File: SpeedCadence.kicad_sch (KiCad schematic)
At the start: 9 parts, among them SW1 SW_Push, U1 STM32F072RBTx

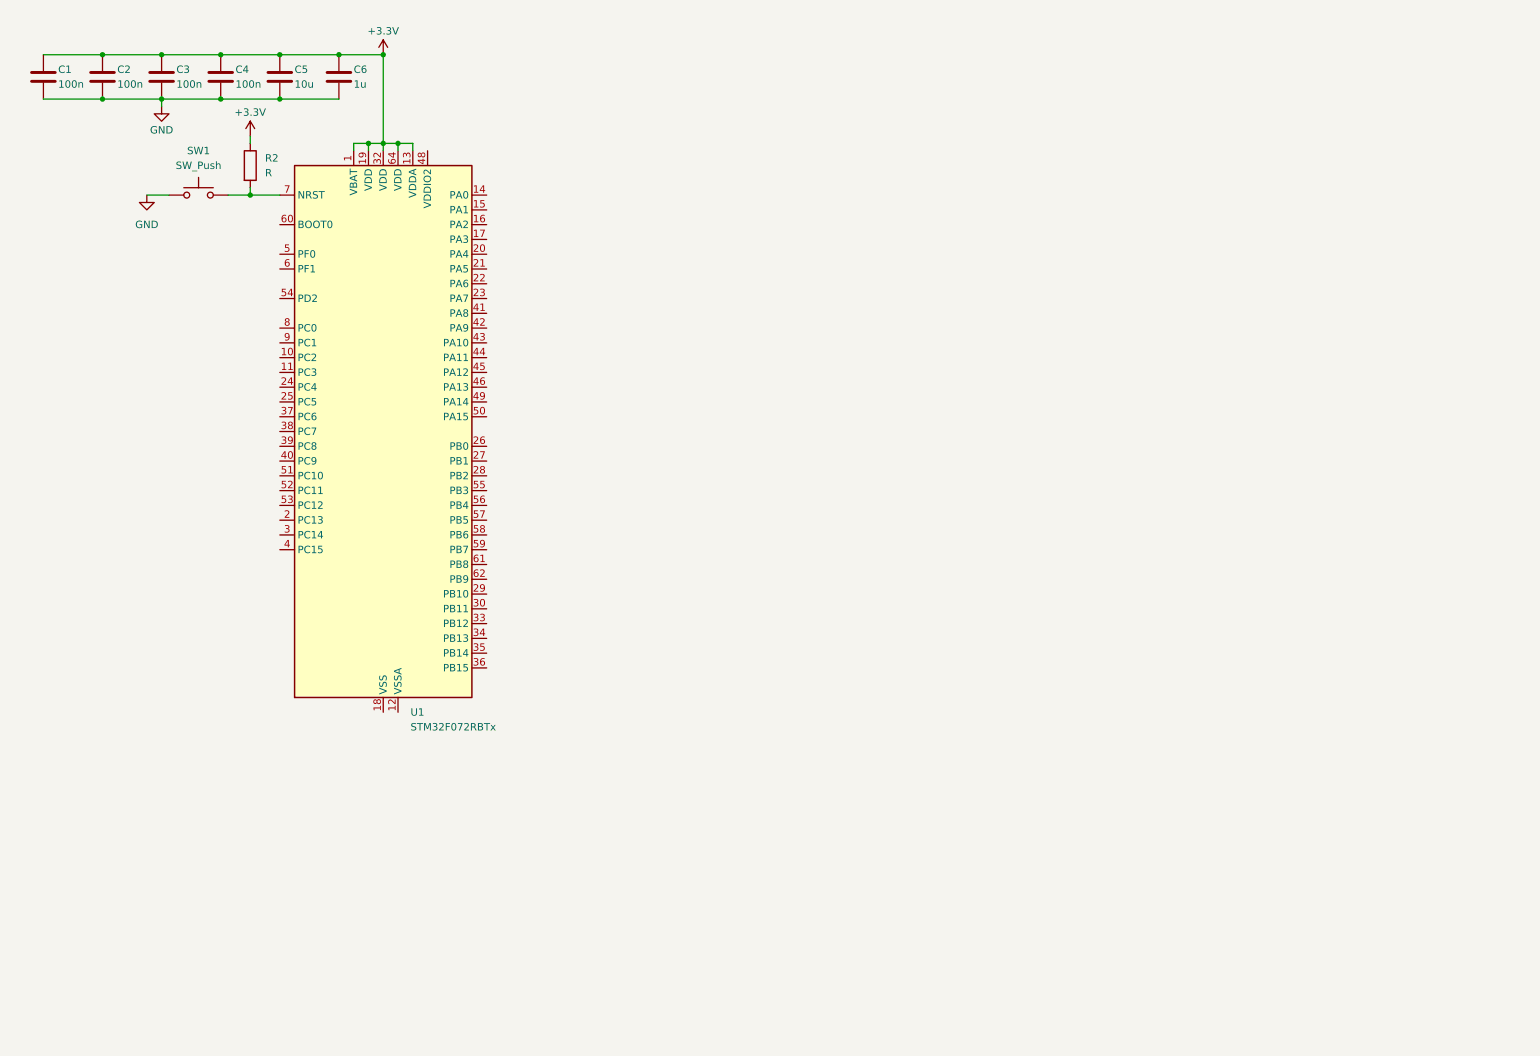
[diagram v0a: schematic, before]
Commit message: Added MCU
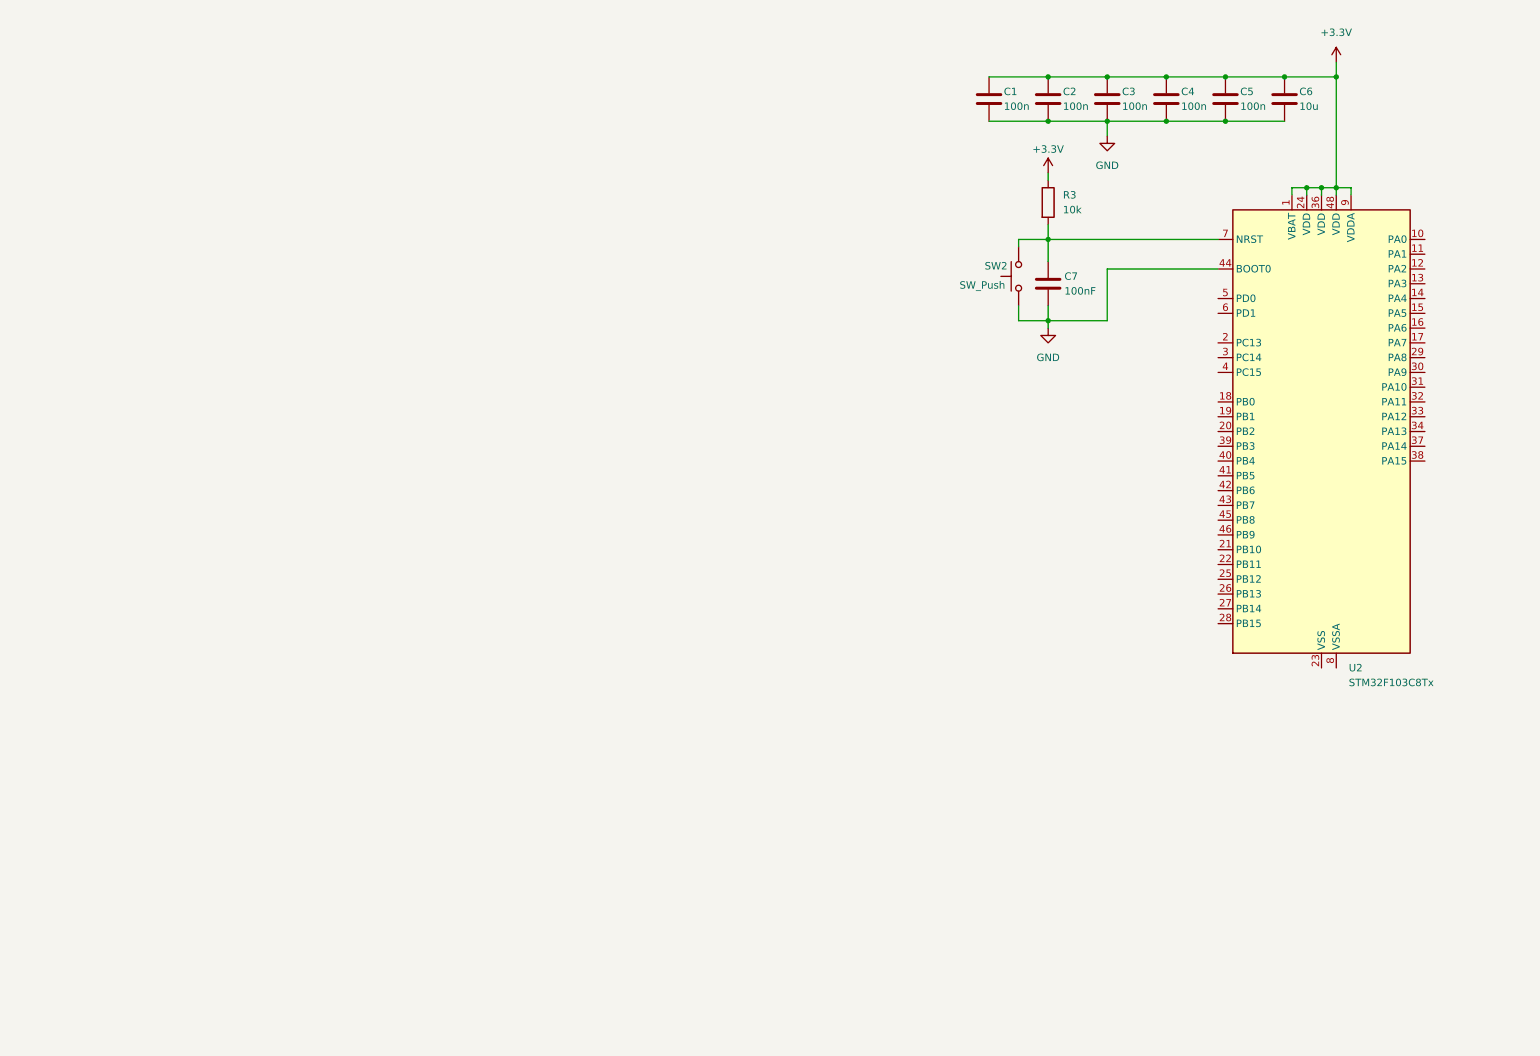
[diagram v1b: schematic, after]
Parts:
- removed R2: R, symbol Device:R
- removed SW1: SW_Push, symbol Switch:SW_Push
- removed U1: STM32F072RBTx, Package_QFP:LQFP-64_10x10mm_P0.5mm, symbol MCU_ST_STM32F0:STM32F072RBTx
- added C7: 100nF, symbol Device:C
- added R3: 10k, symbol Device:R
- added SW2: SW_Push, symbol Switch:SW_Push
- added U2: STM32F103C8Tx, Package_QFP:LQFP-48_7x7mm_P0.5mm, symbol MCU_ST_STM32F1:STM32F103C8Tx
- C5: value 10u -> 100n
- C6: value 1u -> 10u
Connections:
- net +3.3V: now also R3.1, U2.1 (VBAT), U2.24 (VDD), U2.36 (VDD), U2.48 (VDD), U2.9 (VDDA)
- net GND: now also C7.2, SW2.1, U2.44 (BOOT0)
- new net: U2.23 (VSS), U2.35 (VSS), U2.47 (VSS)
- new net: C7.1, R3.2, SW2.2, U2.7 (NRST)
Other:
- moved on the sheet: C1, C2, C3, C4, C5, C6

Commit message: Added connecter and hall effect
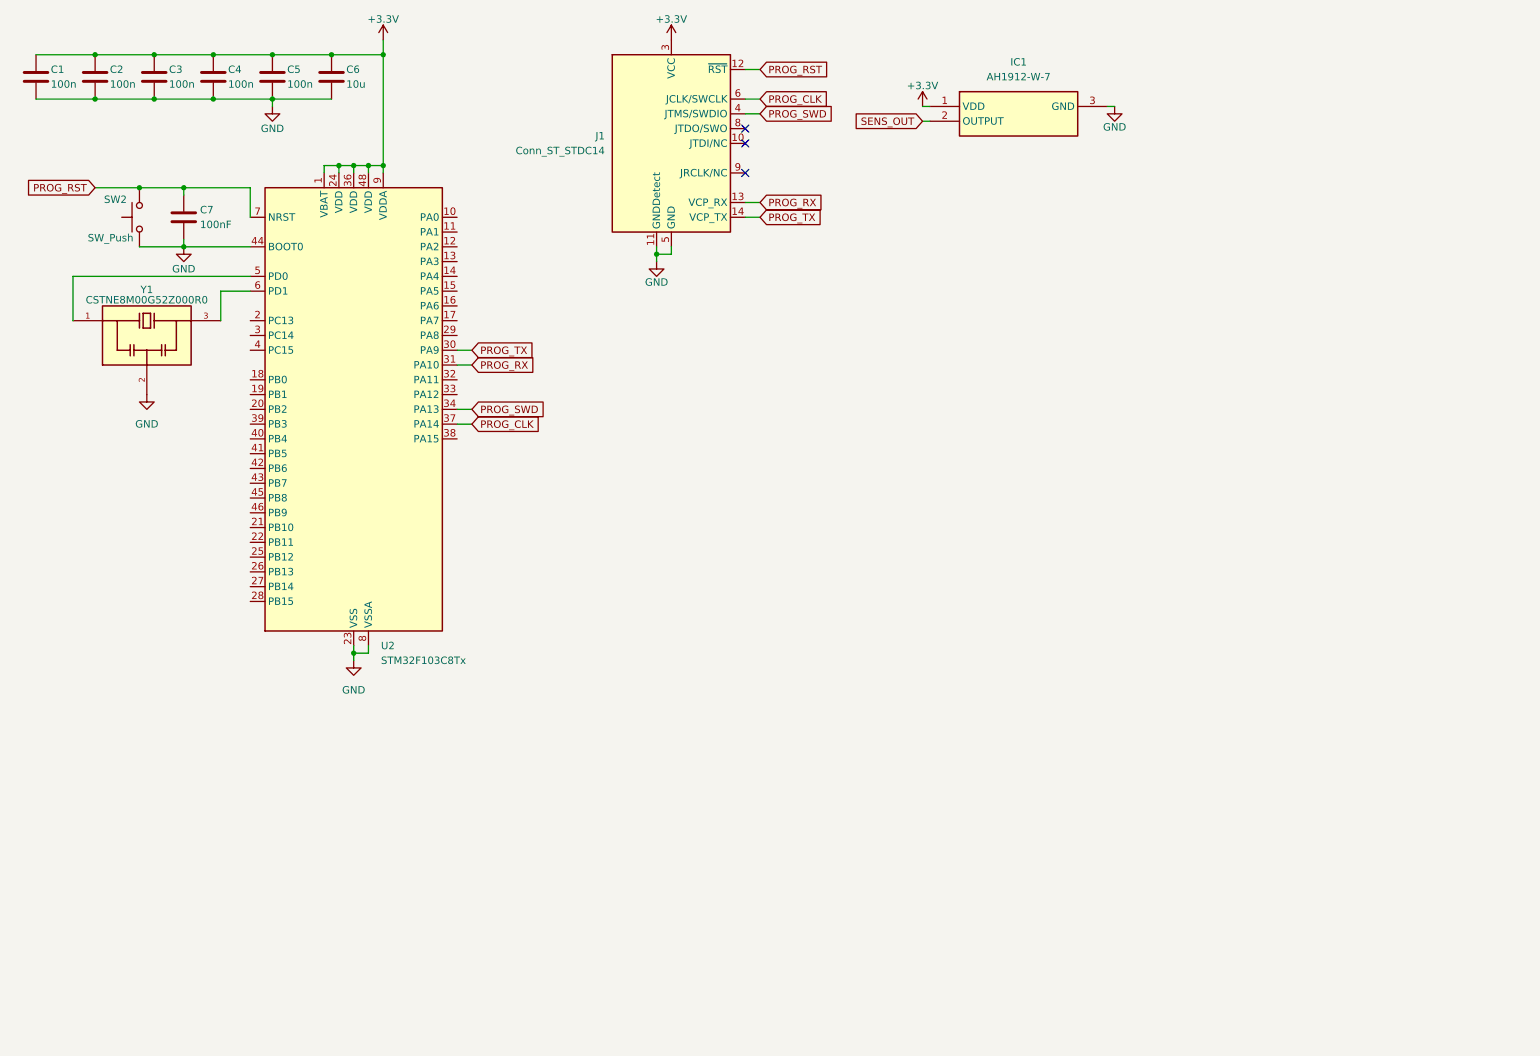
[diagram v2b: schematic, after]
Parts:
- removed R3: 10k, symbol Device:R
- added IC1: AH1912-W-7, Package_TO_SOT_SMD:SOT-23-3, symbol AH1912-W-7:AH1912-W-7
- added J1: Conn_ST_STDC14, symbol Connector:Conn_ST_STDC14
- added Y1: CSTNE8M00G52Z000R0, CSTNE8M00G52Z000R0:OSC_CSTNE8M00G52Z000R0, symbol CSTNE8M00G52Z000R0:CSTNE8M00G52Z000R0
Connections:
- net +3.3V: now also IC1.1 (VDD), J1.3 (VCC)
- net GND: now also U2.23 (VSS), U2.35 (VSS), U2.47 (VSS), U2.8 (VSSA), IC1.3 (GND), J1.11 (GNDDetect), J1.5 (GND), J1.7 (GND), Y1.2
- net PROG_TX: now reaches U2.30 (PA9)
- net PROG_TX: now also J1.14 (VCP_TX)
- net PROG_RX: now reaches U2.31 (PA10)
- net PROG_RX: now also J1.13 (VCP_RX)
- net PROG_SWD: now reaches U2.34 (PA13)
- net PROG_SWD: now also J1.4 (JTMS/SWDIO)
- net PROG_CLK: now reaches U2.37 (PA14)
- net PROG_CLK: now also J1.6 (JCLK/SWCLK)
- net at U2.5 (PD0): now also Y1.1
- net at U2.6 (PD1): now also Y1.3
- net PROG_RST: now reaches C7.1, SW2.2, U2.7 (NRST)
- net PROG_RST: now also J1.12 (~{RST})
- new net SENS_OUT: IC1.2 (OUTPUT)
- no-connect marks 0 -> 3
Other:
- moved on the sheet: C1, C2, C3, C4, C5, C6, C7, SW2, U2

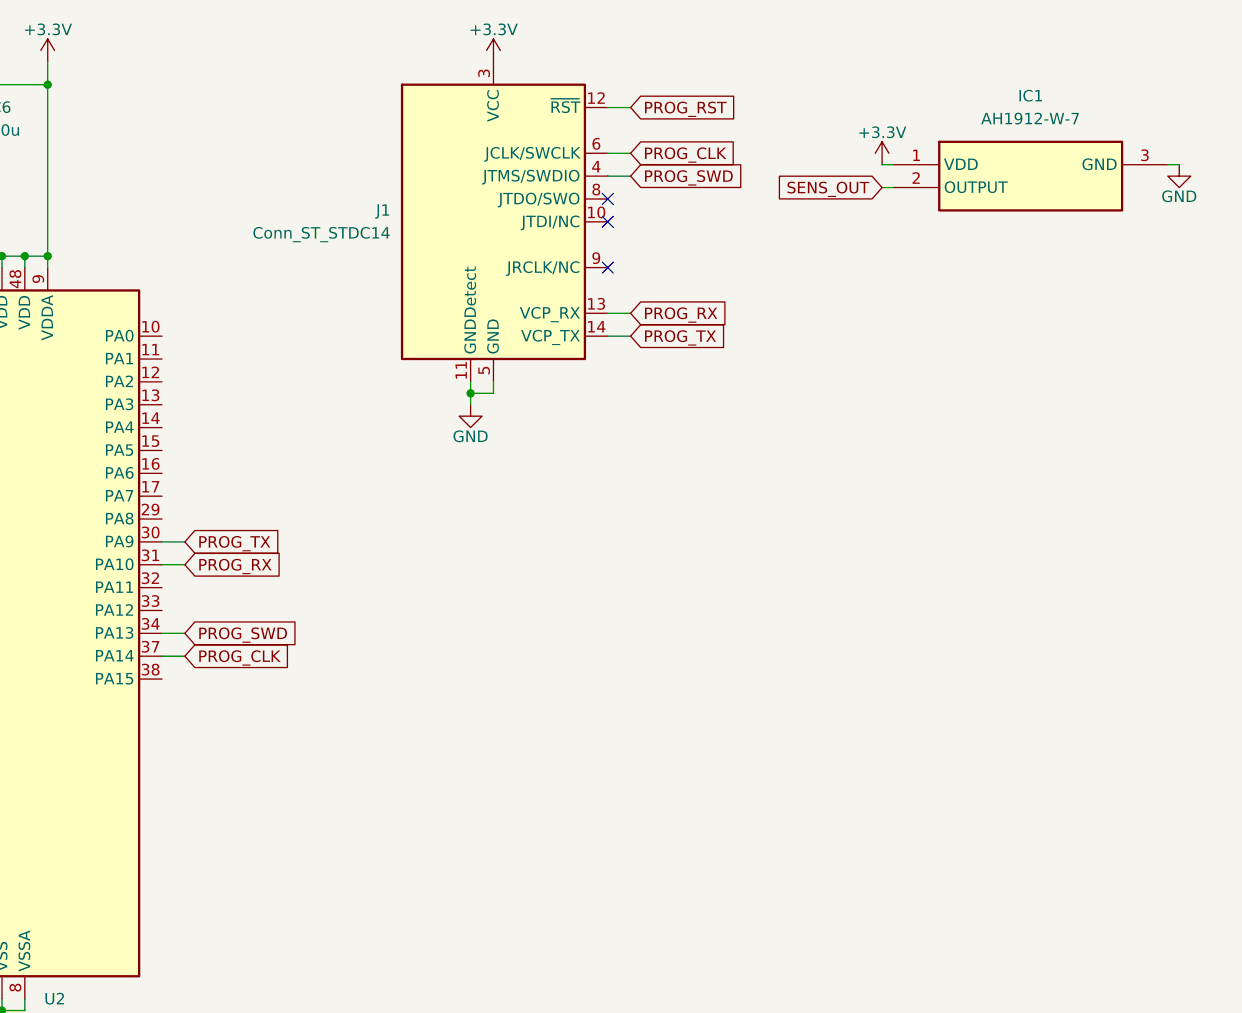
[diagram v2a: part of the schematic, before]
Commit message: Added voltage regulator and USBC
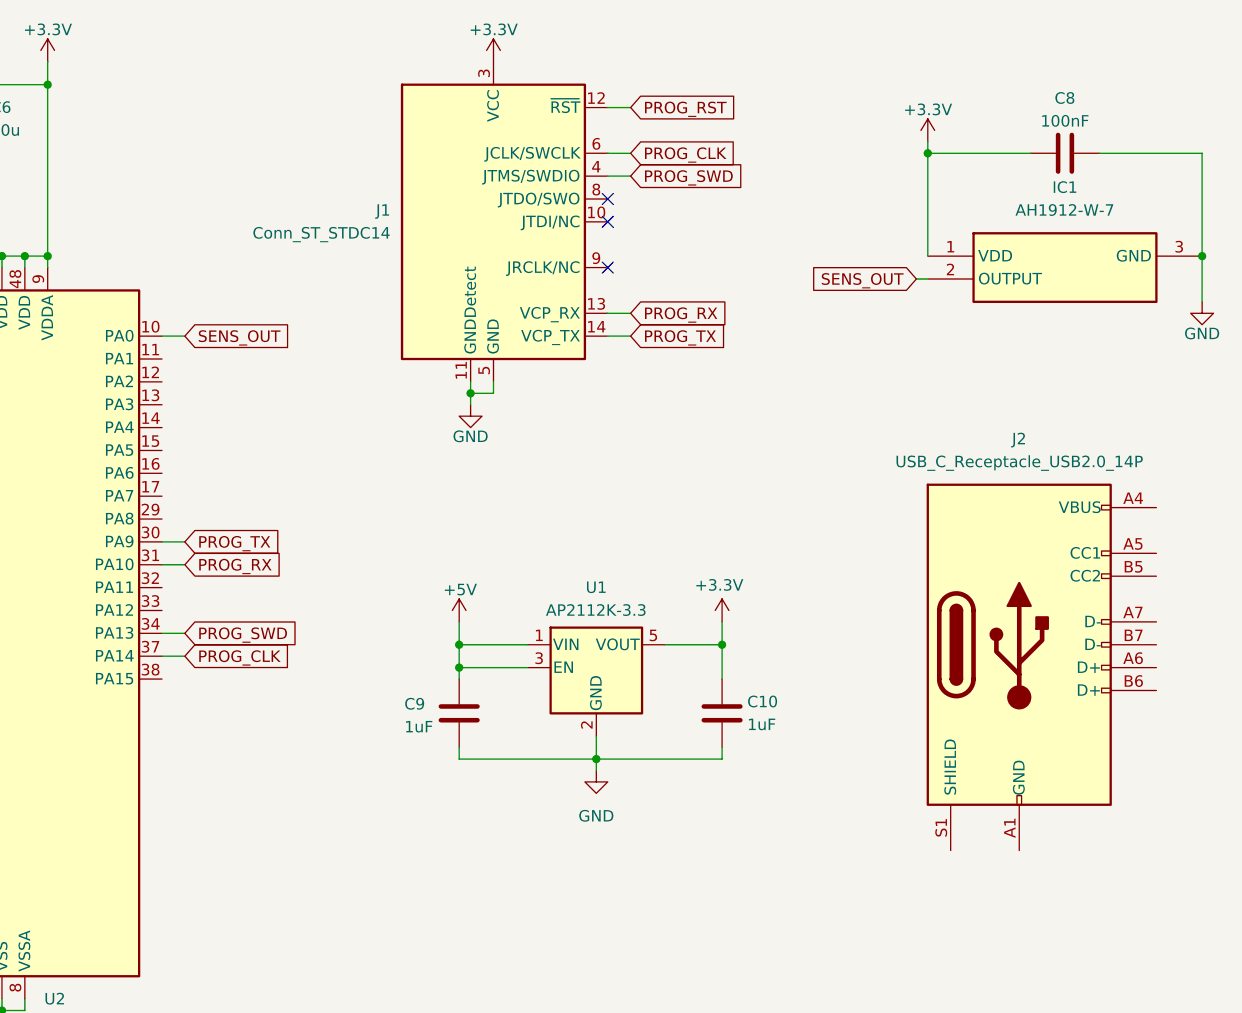
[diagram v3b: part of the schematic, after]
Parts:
- added C10, C9: 1uF, symbol Device:C
- added C8: 100nF, symbol Device:C
- added J2: USB_C_Receptacle_USB2.0_14P, symbol Connector:USB_C_Receptacle_USB2.0_14P
- added U1: AP2112K-3.3, Package_TO_SOT_SMD:SOT-23-5, symbol Regulator_Linear:AP2112K-3.3
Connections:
- net +3.3V: now also C10.1, C8.2, U1.5 (VOUT)
- net GND: now also C10.2, C8.1, C9.2, U1.2 (GND)
- net SENS_OUT: now also U2.10 (PA0)
- new net: J2.A1 (GND), J2.A12 (GND), J2.B1 (GND), J2.B12 (GND)
- new net: J2.A4 (VBUS), J2.A9 (VBUS), J2.B4 (VBUS), J2.B9 (VBUS)
- new net +5V: C9.1, U1.1 (VIN), U1.3 (EN)
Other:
- moved on the sheet: IC1

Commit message: Major changes
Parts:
- removed IC1: AH1912-W-7, Package_TO_SOT_SMD:SOT-23-3, symbol AH1912-W-7:AH1912-W-7
- removed J2: USB_C_Receptacle_USB2.0_14P, symbol Connector:USB_C_Receptacle_USB2.0_14P
- added BT1: XT30, Connector_AMASS:AMASS_XT30PW-M_1x02_P2.50mm_Horizontal, symbol Connector:Conn_01x02_Pin
- added C11: 4.7n, Capacitor_SMD:C_0805_2012Metric, symbol Device:C
- added D1: PTVS5V0Z1USK, Diode_SMD:Nexperia_DSN1608-2_1.6x0.8mm, symbol Diode:PTVS5V0Z1USK
- added D2, D3: D_Schottky, Diode_SMD:D_SOD-123, symbol Device:D_Schottky
- added F1: Polyfuse, Fuse:Fuse_1206_3216Metric, symbol Device:Polyfuse
- added J2: USB_C_Receptacle_USB2.0_16P, Connector_USB:USB_C_Receptacle_HRO_TYPE-C-31-M-12, symbol Connector:USB_C_Receptacle_USB2.0_16P
- added J3: Conn_01x03_Pin, Connector_JST:JST_XH_B3B-XH-A_1x03_P2.50mm_Vertical, symbol Connector:Conn_01x03_Pin
- added J4: Conn_01x02_Pin, Connector_JST:JST_XH_B2B-XH-A_1x02_P2.50mm_Vertical, symbol Connector:Conn_01x02_Pin
- added J5: Conn_01x04_Pin, Connector_JST:JST_XH_B4B-XH-A_1x04_P2.50mm_Vertical, symbol Connector:Conn_01x04_Pin
- added R1, R2: 5.1k, Resistor_SMD:R_0805_2012Metric, symbol Device:R
- added R3, R4: 60, Resistor_SMD:R_0805_2012Metric, symbol Device:R
- added U3: TCAN3414DR, Package_SO:SOIC-8_3.9x4.9mm_P1.27mm, symbol TCAN3414:PTCAN3414DR
- C1, C2, C3, C4, C5, C6: footprint (none) -> Capacitor_SMD:C_0805_2012Metric
- C10, C9: value 1uF -> 1u; footprint (none) -> Capacitor_SMD:C_0805_2012Metric
- C7, C8: value 100nF -> 100n; footprint (none) -> Capacitor_SMD:C_0805_2012Metric
- J1: footprint (none) -> Connector_PinHeader_1.27mm:PinHeader_2x07_P1.27mm_Vertical_SMD
- SW2: footprint (none) -> Button_Switch_SMD:SW_SPST_SKQG_WithStem
- Y1: footprint CSTNE8M00G52Z000R0:OSC_CSTNE8M00G52Z000R0 -> OSC_CST:OSC_CSTNE8M00G52Z000R0
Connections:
- net +3.3V: now also C8.1, J3.1 (Pin_1), J5.1 (Pin_1), U3.3 (VCC); no longer C8.2
- net +5V: now also D2.1 (K), D3.1 (K)
- net SENS_OUT: now also J3.3 (Pin_3)
- net STB: now reaches U2.18 (PB0)
- net STB: now also U3.8 (STB)
- net SHDN: now reaches U2.19 (PB1)
- net SHDN: now also U3.5 (SHDN)
- net CAN_RX: now reaches U2.32 (PA11)
- net CAN_RX: now also U3.4 (RXD)
- net CAN_TX: now reaches U2.33 (PA12)
- net CAN_TX: now also U3.1 (TXD)
- net OLED_SCL: now reaches U2.42 (PB6)
- net OLED_SCL: now also U2.43 (PB7), J5.3 (Pin_3)
- net GND renamed +5V_BATT
- net +5V_BATT: now also C8.2, BT1.1 (Pin_1), BT1.2 (Pin_2), C11.2, D1.2 (A), D3.2 (A), J2.A1 (GND), J2.A12 (GND), J2.B1 (GND), J2.B12 (GND), J3.2 (Pin_2), J5.2 (Pin_2), R1.2, R2.2, U3.2 (GND); no longer C8.1
- new net: C11.1, R3.2, R4.1
- new net: J2.A5 (CC1), R1.1
- new net: F1.2, J2.A4 (VBUS), J2.A9 (VBUS), J2.B4 (VBUS), J2.B9 (VBUS)
- new net: J2.B5 (CC2), R2.1
- new net +5V_USB: D1.1 (K), D2.2 (A), F1.1
- new net CANH: J4.1 (Pin_1), R3.1, U3.7 (CANH)
- new net CANL: J4.2 (Pin_2), R4.2, U3.6 (CANL)
- new net OLED_SDA: J5.4 (Pin_4)
- no-connect marks 3 -> 10
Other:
- note added: "Battery Header"
- note added: "CAN Bus Header"
- note added: "CAN Transciever"
- note added: "Hall Effect Sensor Header"
- note added: "LDO Voltage Regulator (5V to 3.3V)"
- note added: "MCU - STM32F103"
- note added: "OLED Display Header"
- note added: "Power Source"
- note added: "Programming Header"
- note added: "USB-C 2.0 Header"
- moved on the sheet: C1, C10, C2, C3, C4, C5, C6, C9, J1, U1
